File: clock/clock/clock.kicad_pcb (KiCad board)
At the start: 2 copper layers, 55 x 110 mm, 44 parts, among them J1 AVR-ISP-6, J10 Conn_01x05_Male, J11 CV_IN, J12 CLOCK_OUT, J13 SUBDIV_OUT, J2 EURORACK_CONN_10, J3 Conn_01x05_Female, J4 Conn_01x05_Male, J5 Conn_01x05_Female, J6 Conn_01x05_Male, J7 Conn_01x05_Female, J8 Conn_01x05_Male, J9 Conn_01x05_Female, SW1 SW_Push, SW2 SW_Push, SW3 SW_Coded_SH-7050, U1 ATmega328P-PU, U2 L7805, U3 SM460281N, U4 SM460281N, U5 SM460281N, Y1 16MHz

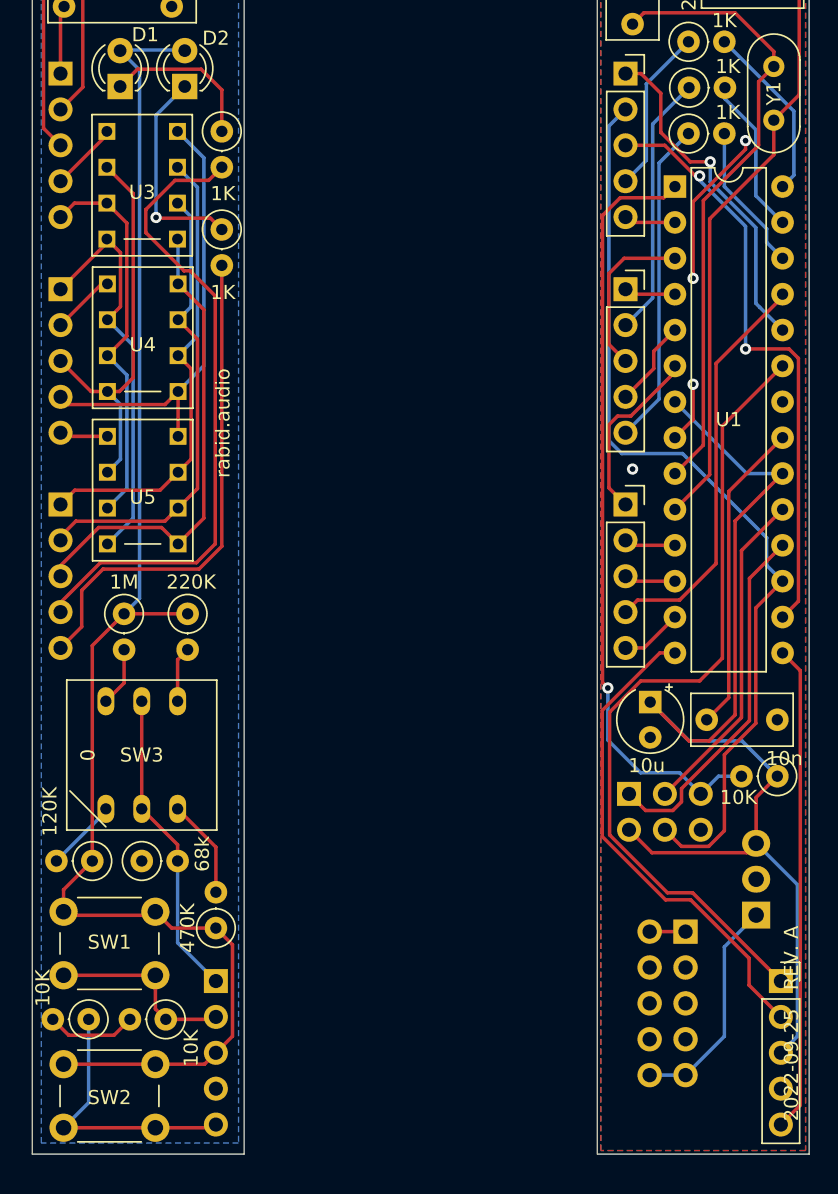
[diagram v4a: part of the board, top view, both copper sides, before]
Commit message: simplify some complex routing
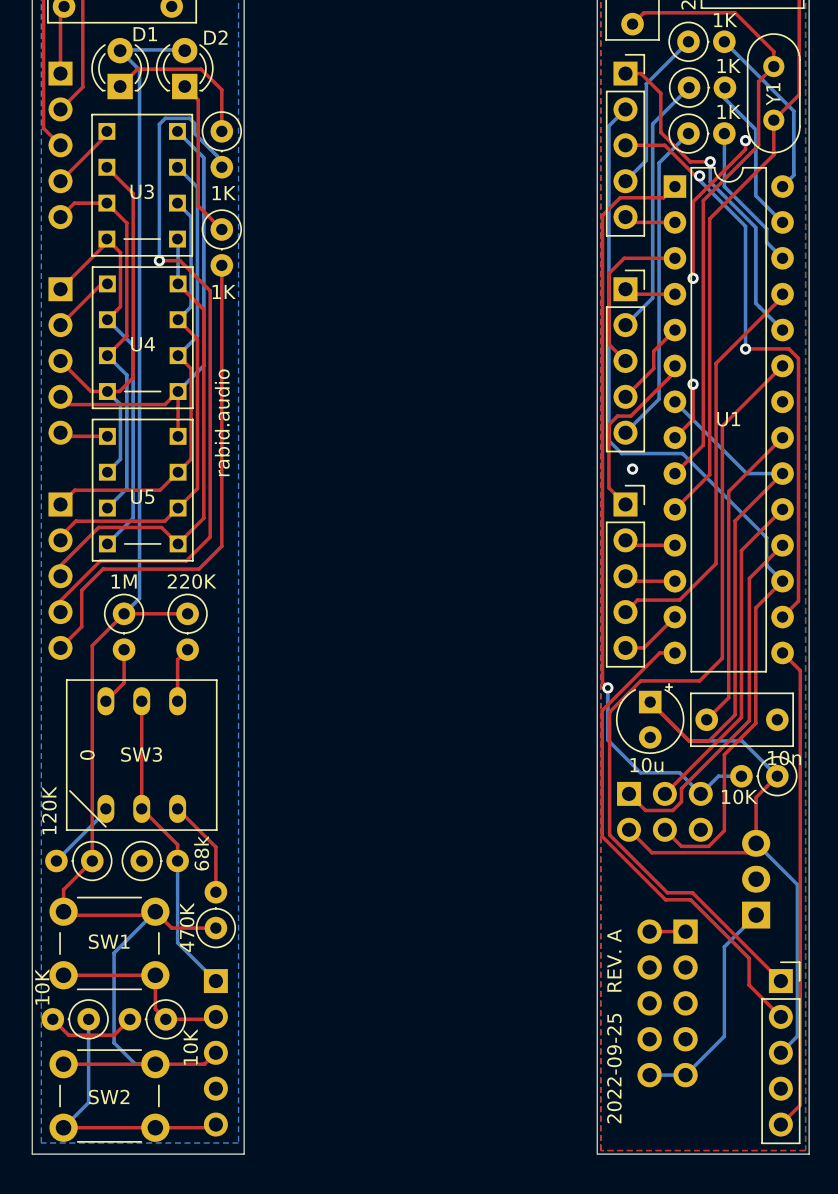
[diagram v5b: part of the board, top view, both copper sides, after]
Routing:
- net /LED_A: track 46.3 -> 52.6 mm, vias 0 -> 1
- net /AVCC: track 105.0 -> 109.3 mm
- net Net-(D2-Pad1): track 15.8 -> 11.9 mm, vias 1 -> 0
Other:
- board text removed: "TODO: confirm pot orientation"
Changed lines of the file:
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@@
   (general
     (thickness 1.6)
-    (drawings 13)
-    (tracks 342)
+    (drawings 12)
+    (tracks 344)
     (zones 0)
     (modules 44)
@@
     (effects (font (size 1 1) (thickness 0.15)) (justify mirror))
   )
-  (gr_text "2022-09-25   REV. A" (at 53.75 100.75 90) (layer F.SilkS)
+  (gr_text "2022-09-25   REV. A" (at 41.25 101 90) (layer F.SilkS)
     (effects (font (size 1 1) (thickness 0.15)))
   )
   (gr_text rabid.audio (at 13.5 58.25 90) (layer F.SilkS)
-    (effects (font (size 1 1) (thickness 0.15)))
-  )
-  (gr_text "TODO: confirm pot orientation" (at 12 117.5) (layer Dwgs.User)
     (effects (font (size 1 1) (thickness 0.15)))
   )
@@
   (segment (start 54.299999 35.000001) (end 54.299999 27.799999) (width 0.25) (layer F.Cu) (net 5))
   (segment (start 52.5 36.8) (end 54.299999 35.000001) (width 0.25) (layer F.Cu) (net 5) (status 10))
+  (segment (start 13.42 37.592) (end 13.42 34.656998) (width 0.25) (layer F.Cu) (net 6) (status 10))
+  (segment (start 13.42 34.656998) (end 11.955001 33.191999) (width 0.25) (layer F.Cu) (net 6))
   (segment (start 7.445001 33.191999) (end 6.22 34.417) (width 0.25) (layer F.Cu) (net 6) (status 20))
   (segment (start 11.955001 33.191999) (end 7.445001 33.191999) (width 0.25) (layer F.Cu) (net 6))
-  (segment (start 13.42 34.656998) (end 11.955001 33.191999) (width 0.25) (layer F.Cu) (net 6))
-  (segment (start 13.42 37.592) (end 13.42 34.656998) (width 0.25) (layer F.Cu) (net 6) (status 10))
   (segment (start 10.82 35.03) (end 10.82 34.37) (width 0.25) (layer F.Cu) (net 7) (status 30))
-  (segment (start 8.815001 43.740001) (end 8.763 43.688) (width 0.25) (layer F.Cu) (net 7))
-  (via (at 8.763 43.688) (size 0.8) (drill 0.4) (layers F.Cu B.Cu) (net 7))
-  (segment (start 12.620001 43.740001) (end 8.815001 43.740001) (width 0.25) (layer F.Cu) (net 7))
-  (segment (start 13.42 44.54) (end 12.620001 43.740001) (width 0.25) (layer F.Cu) (net 7) (status 10))
-  (segment (start 8.763 43.688) (end 8.763 36.449) (width 0.25) (layer B.Cu) (net 7))
-  (segment (start 8.763 36.449) (end 10.795 34.417) (width 0.25) (layer B.Cu) (net 7) (status 20))
+  (segment (start 13.42 44.54) (end 11.75 42.87) (width 0.25) (layer F.Cu) (net 7))
+  (segment (start 11.75 35.372) (end 10.795 34.417) (width 0.25) (layer F.Cu) (net 7))
+  (segment (start 11.75 42.87) (end 11.75 35.372) (width 0.25) (layer F.Cu) (net 7))
   (segment (start 44.704999 42.295001) (end 45.5 41.5) (width 0.25) (layer F.Cu) (net 8) (status 30))
   (segment (start 41.625997 42.295001) (end 44.704999 42.295001) (width 0.25) (layer F.Cu) (net 8) (status 20))
@@
   (segment (start 0.798999 6.470001) (end 0.798999 37.378999) (width 0.25) (layer F.Cu) (net 14))
   (segment (start 2.189 5.08) (end 0.798999 6.470001) (width 0.25) (layer F.Cu) (net 14) (status 10))
-  (segment (start 11.180001 47.464999) (end 12.954 49.238998) (width 0.25) (layer F.Cu) (net 15))
-  (segment (start 10.109997 41.060001) (end 8.037999 43.131999) (width 0.25) (layer F.Cu) (net 15))
-  (segment (start 13.42 40.132) (end 12.491999 41.060001) (width 0.25) (layer F.Cu) (net 15) (status 10))
-  (segment (start 12.491999 41.060001) (end 10.109997 41.060001) (width 0.25) (layer F.Cu) (net 15))
-  (segment (start 12.954 49.238998) (end 12.954 66.80059) (width 0.25) (layer F.Cu) (net 15))
-  (segment (start 12.954 66.80059) (end 11.6246 68.12999) (width 0.25) (layer F.Cu) (net 15))
-  (segment (start 8.037999 44.758001) (end 8.037999 43.131999) (width 0.25) (layer F.Cu) (net 15))
-  (segment (start 10.744997 47.464999) (end 8.037999 44.758001) (width 0.25) (layer F.Cu) (net 15))
-  (segment (start 11.180001 47.464999) (end 10.744997 47.464999) (width 0.25) (layer F.Cu) (net 15))
   (segment (start 2.105 71.885) (end 2.105 71.489998) (width 0.25) (layer F.Cu) (net 15) (status 30))
   (segment (start 2 70.958588) (end 2 71.628) (width 0.25) (layer F.Cu) (net 15) (status 30))
-  (segment (start 4.828597 68.129991) (end 2 70.958588) (width 0.25) (layer F.Cu) (net 15) (status 20))
-  (segment (start 11.6246 68.12999) (end 4.828597 68.129991) (width 0.25) (layer F.Cu) (net 15))
+  (segment (start 2 70.827002) (end 4.827002 68) (width 0.25) (layer F.Cu) (net 15))
+  (segment (start 2 71.628) (end 2 70.827002) (width 0.25) (layer F.Cu) (net 15))
+  (segment (start 10.910002 68) (end 12.595029 66.314973) (width 0.25) (layer F.Cu) (net 15))
+  (segment (start 4.827002 68) (end 10.910002 68) (width 0.25) (layer F.Cu) (net 15))
+  (segment (start 12.595029 66.314973) (end 12.595029 48.880027) (width 0.25) (layer F.Cu) (net 15))
+  (segment (start 13.42 40.132) (end 13.42 39.67) (width 0.25) (layer B.Cu) (net 15))
+  (segment (start 13.42 39.67) (end 11.5 37.75) (width 0.25) (layer B.Cu) (net 15))
+  (via (at 9 46.75) (size 0.8) (drill 0.4) (layers F.Cu B.Cu) (net 15))
+  (segment (start 11.140001 36.669999) (end 9.419999 36.669999) (width 0.25) (layer B.Cu) (net 15))
+  (segment (start 9 37.089998) (end 9 46.75) (width 0.25) (layer B.Cu) (net 15))
+  (segment (start 11.5 37.75) (end 11.5 37.029998) (width 0.25) (layer B.Cu) (net 15))
+  (segment (start 9.419999 36.669999) (end 9 37.089998) (width 0.25) (layer B.Cu) (net 15))
+  (segment (start 11.5 37.029998) (end 11.140001 36.669999) (width 0.25) (layer B.Cu) (net 15))
+  (segment (start 10.465002 46.75) (end 12.595029 48.880027) (width 0.25) (layer F.Cu) (net 15))
+  (segment (start 9 46.75) (end 10.465002 46.75) (width 0.25) (layer F.Cu) (net 15))
   (segment (start 13.42 66.971) (end 13.42 47.08) (width 0.25) (layer F.Cu) (net 16) (status 20))
   (segment (start 11.811 68.58) (end 13.42 66.971) (width 0.25) (layer F.Cu) (net 16))
@@
   (segment (start 12.194 103.636) (end 13 102.83) (width 0.25) (layer F.Cu) (net 31))
   (segment (start 8.715 103.636) (end 12.194 103.636) (width 0.25) (layer F.Cu) (net 31))
-  (segment (start 14.175001 95.175001) (end 13 94) (width 0.25) (layer F.Cu) (net 31))
-  (segment (start 14.175001 101.654999) (end 14.175001 95.175001) (width 0.25) (layer F.Cu) (net 31))
-  (segment (start 13 102.83) (end 14.175001 101.654999) (width 0.25) (layer F.Cu) (net 31))
   (segment (start 9.874 94) (end 8.715 92.841) (width 0.25) (layer F.Cu) (net 31))
   (segment (start 13 94) (end 9.874 94) (width 0.25) (layer F.Cu) (net 31))
@@
   (segment (start 4.25 74) (end 6.5 71.75) (width 0.25) (layer F.Cu) (net 31))
   (segment (start 4.25 89.25) (end 4.25 74) (width 0.25) (layer F.Cu) (net 31))
+  (segment (start 5.788999 102.124212) (end 5.788999 95.767001) (width 0.25) (layer B.Cu) (net 31))
+  (segment (start 5.788999 95.767001) (end 8.715 92.841) (width 0.25) (layer B.Cu) (net 31))
+  (segment (start 7.300787 103.636) (end 5.788999 102.124212) (width 0.25) (layer B.Cu) (net 31))
+  (segment (start 8.715 103.636) (end 7.300787 103.636) (width 0.25) (layer B.Cu) (net 31))
   (segment (start 41.737999 60.405001) (end 40.824999 59.492001) (width 0.25) (layer B.Cu) (net 32))
   (segment (start 46.040001 60.405001) (end 41.737999 60.405001) (width 0.25) (layer B.Cu) (net 32))

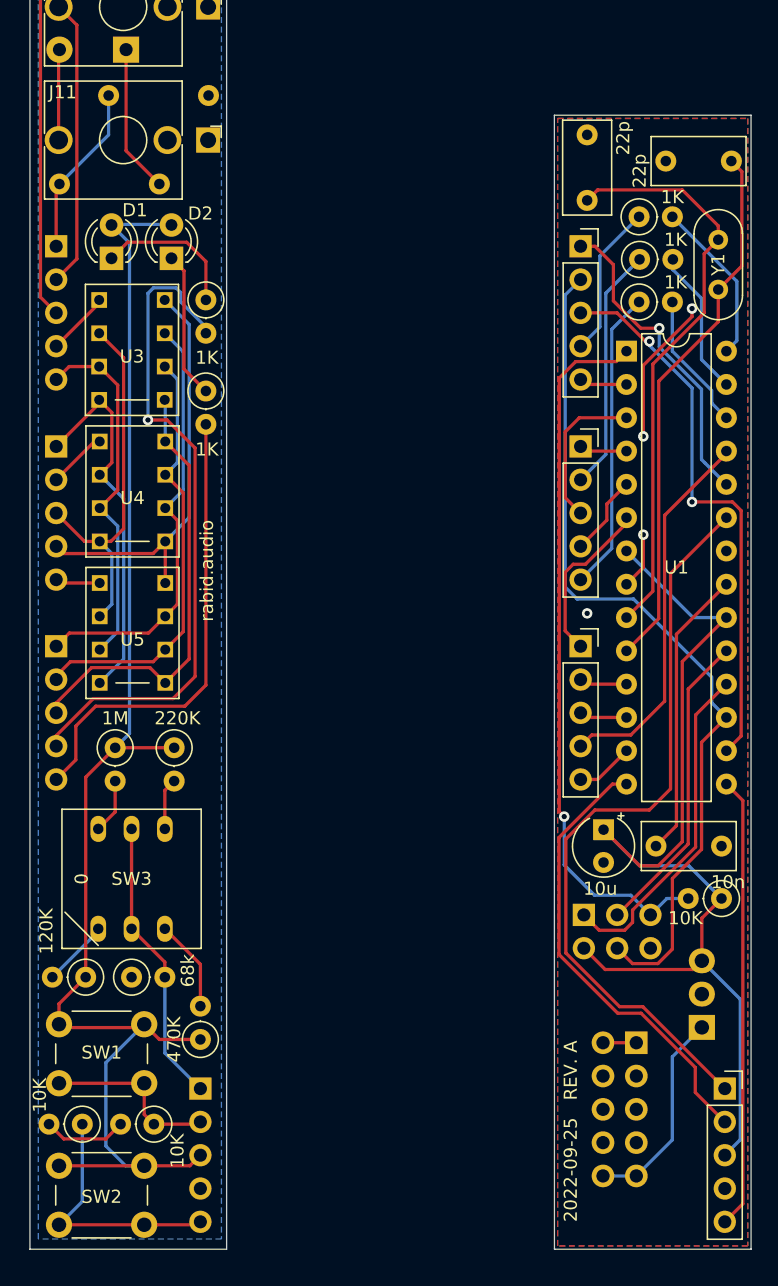
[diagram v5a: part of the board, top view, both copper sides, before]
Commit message: redesign pcb around rotary encoder
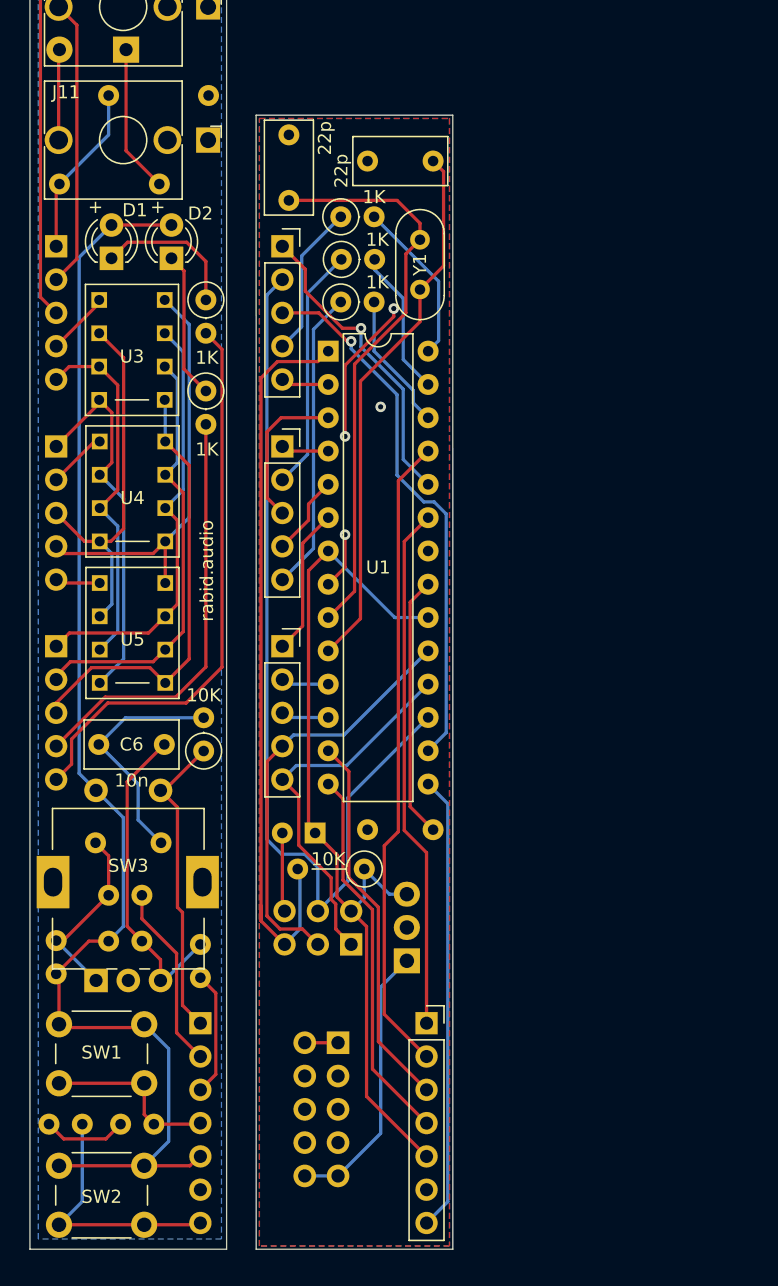
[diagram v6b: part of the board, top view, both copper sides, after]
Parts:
- added C5: 10n, Capacitor_THT:C_Rect_L7.0mm_W3.5mm_P5.00mm, B.Cu at (5.00, 79.0)
- added C6: 10n, Capacitor_THT:C_Rect_L7.0mm_W3.5mm_P5.00mm, F.Cu at (10.2, 71.5)
- C1, C2, R4, R5: moved to B.Cu
- J1: value AVR-ISP-6 -> AVR-ISP
- J10: value Conn_01x05_Male -> Conn_01x07_Male; footprint Connector_PinHeader_2.54mm:PinHeader_1x05_P2.54mm_Vertical -> Connector_PinHeader_2.54mm:PinHeader_1x07_P2.54mm_Vertical
- J9: value Conn_01x05_Female -> Conn_01x07_Female; footprint Connector_PinSocket_2.54mm:PinSocket_1x05_P2.54mm_Vertical -> Connector_PinSocket_2.54mm:PinSocket_1x07_P2.54mm_Vertical
- R1: footprint Resistor_THT:R_Axial_DIN0207_L6.3mm_D2.5mm_P2.54mm_Vertical -> Resistor_THT:R_Axial_DIN0207_L6.3mm_D2.5mm_P5.08mm_Vertical
- R10: value 220K -> 10K; moved to B.Cu
- R11: value 470K -> 10K; moved to B.Cu
- R12: value 1M -> 10K; moved to B.Cu
- R13: value 68k -> 10K
- R9: value 120K -> 10K; moved to B.Cu
- SW3: value SW_Coded_SH-7050 -> Rotary_Encoder_Switch; footprint synth:SD-1110 -> synth:RotaryEncoder_Bourns_PEC11H_Vertical_Switch
- moved R1 27.3 mm to (25.5, 81.0)
- moved C2 27.0 mm to (25.8, 78.0), turned to 0 degrees
- moved J9 23.3 mm to (30.2, 92.8)
- moved U2 23.1 mm to (28.8, 88.0)
- moved C3 22.8 mm to (19.8, 25.0)
- moved C4 22.8 mm to (25.8, 27.0)
- moved J2 22.8 mm to (23.5, 94.2)
- moved J3 22.8 mm to (19.2, 33.5)
- moved J5 22.8 mm to (19.2, 48.8)
- moved J7 22.8 mm to (19.2, 64.0)
- moved R6 22.8 mm to (23.7, 37.8)
- moved R7 22.8 mm to (23.8, 34.5)
- moved R8 22.8 mm to (23.7, 31.2)
- moved U1 22.8 mm to (22.8, 41.5)
- moved Y1 22.8 mm to (29.8, 33.0)
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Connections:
- net /B_KNOB renamed /B_SW3
- J1 pad 1: /MISO -> /B_LEDL
- J1 pad 3: /SCK -> /B_LEDR
- J10 pad 1: /KNOB -> /SW3
- J10 pad 2: /SW1 -> /KNOBL
- J10 pad 3: /AVCC -> /KNOBR
- J10 pad 4: /AGND -> /SW1
- J10 pad 5: /SW2 -> /AVCC
- J7 pad 4: /B_LED_A -> /B_LEDR
- J7 pad 5: /B_LED_B -> /B_LEDL
- J8 pad 4: /LED_A -> /LEDR
- J8 pad 5: /LED_B -> /LEDL
- J9 pad 2: /B_SW1 -> /B_KNOBL
- J9 pad 3: +5V -> /B_KNOBR
- J9 pad 4: GND -> /B_SW1
- J9 pad 5: /B_SW2 -> +5V
- R10 pad 2: Net-(R10-Pad2) -> Net-(C5-Pad1)
- R11 pad 2: Net-(R11-Pad2) -> Net-(C6-Pad1)
- R12 pad 1: /AVCC -> Net-(C6-Pad1)
- R12 pad 2: Net-(R12-Pad2) -> /KNOBR
- R13 pad 1: /AGND -> /SW3
- R13 pad 2: /KNOB -> /AGND
- R2 pad 2: /LED_A -> /LEDL
- R3 pad 2: /LED_B -> /LEDR
- R9 pad 1: /AVCC -> Net-(C5-Pad1)
- R9 pad 2: Net-(R9-Pad2) -> /KNOBL
- SW3 pad 1: Net-(R9-Pad2) -> Net-(C5-Pad1)
- SW3 pad 2: Net-(R10-Pad2) -> /AGND
- SW3 pad 4: Net-(R11-Pad2) -> /SW3
- U1 pad 13: /B_LED_B -> /B_KNOBR
- U1 pad 18: /MISO -> /B_LEDL
- U1 pad 19: /SCK -> /B_LEDR
- U1 pad 25: /B_LED_A -> /B_KNOBL
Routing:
- net /LED_A: track 52.6 -> 0.00 mm, vias 1 -> 0
- net /B_KNOBL: track 0.00 -> 48.9 mm
- net /LEDL: track 0.00 -> 43.3 mm
- net /LED_B: track 35.8 -> 0.00 mm
- net /LEDR: track 0.00 -> 33.1 mm
- net /B_LEDR: track 0.00 -> 32.4 mm
- net /B_KNOBR: track 0.00 -> 29.0 mm
- net /B_LEDL: track 0.00 -> 28.9 mm
- net /B_LED_A: track 28.9 -> 0.00 mm
- net /MISO: track 25.6 -> 0.00 mm
- net Net-(C6-Pad1): track 0.00 -> 25.4 mm
- net /SW3: track 0.00 -> 23.8 mm
- net /SCK: track 23.6 -> 0.00 mm
- net /KNOB: track 22.0 -> 0.00 mm
- net /AGND: track 6.39 -> 24.7 mm
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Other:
- board size 55 x 110 mm -> 32.3 x 110 mm
- board text added: "+"
- board text added: "2022-11-24 REV. A"
- board text removed: "2022-09-25 REV. A"

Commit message: make a bit more space
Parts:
- J1: value AVR-ISP -> ISP
- R1: moved to B.Cu
- moved R1 6.18 mm to (24.0, 87.0)
- moved J1 3.25 mm to (24.5, 83.5)
- moved U1 2.51 mm to (23.0, 39.0)
- moved Y1 2.51 mm to (30.0, 30.5)
- moved C1 2.15 mm to (23.0, 76.5)
- moved R6 2.02 mm to (24.0, 35.8)
- moved R8 2.02 mm to (24.0, 29.2)
- moved R7 2.02 mm to (24.0, 32.5)
- moved C4 1.52 mm to (26.0, 25.5)
- moved C2 1.50 mm to (25.8, 76.5)
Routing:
- net GND: track 21.6 -> 12.6 mm, vias 4 -> 2
- net /B_SUBDIV_OUT: track 70.7 -> 63.7 mm
- net /B_SW3: track 40.0 -> 42.6 mm
- net /B_LED3: track 6.18 -> 8.78 mm
- net /B_KNOBL: track 48.9 -> 51.5 mm
- net /B_KNOBR: track 29.0 -> 31.4 mm
- net /B_SW1: track 29.0 -> 31.4 mm
- net /B_LED4: track 11.7 -> 13.9 mm
- net /B_LED_C3: track 23.0 -> 25.1 mm
- net /B_LED_C1: track 11.7 -> 13.8 mm
- net /B_LED_C2: track 18.7 -> 20.8 mm
- net /B_CV_IN: track 24.3 -> 22.4 mm
- net Net-(R8-Pad2): track 13.2 -> 11.4 mm
- net /B_SW2: track 35.5 -> 37.2 mm
- net /B_LEDR: track 32.4 -> 34.0 mm
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
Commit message: fix PCB
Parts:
- removed R12, R9: 10K, Resistor_THT:R_Axial_DIN0207_L6.3mm_D2.5mm_P2.54mm_Vertical
- C3, C4, C6, R6, R7, R8, Y1: moved to B.Cu
- J1: value ISP -> AVR-ISP-6
- SW3: footprint synth:RotaryEncoder_Bourns_PEC11H_Vertical_Switch -> synth:RotaryEncoder_Bourns_PEC11R_Vertical_Switch
- moved C3 0.35 mm to (19.5, 25.2)
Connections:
- C5 pad 1: Net-(C5-Pad1) -> /KNOBL
- C6 pad 1: Net-(C6-Pad1) -> /KNOBR
- D1 pad 1: Net-(D1-Pad1) -> /AGND
- D1 pad 2: /AVCC -> Net-(D1-Pad2)
- D2 pad 1: Net-(D2-Pad1) -> /AGND
- D2 pad 2: /AVCC -> Net-(D2-Pad2)
- J10 pad 1: /SW3 -> /KNOBR
- J10 pad 3: /KNOBR -> /SW3
- J9 pad 1: /B_SW3 -> /B_KNOBR
- J9 pad 3: /B_KNOBR -> /B_SW3
- R10 pad 2: Net-(C5-Pad1) -> /KNOBL
- R11 pad 2: Net-(C6-Pad1) -> /KNOBR
- R2 pad 1: Net-(D1-Pad1) -> Net-(D1-Pad2)
- R3 pad 1: Net-(D2-Pad1) -> Net-(D2-Pad2)
- SW3 pad 1: Net-(C5-Pad1) -> /KNOBL
- SW3 pad 3: Net-(C6-Pad1) -> /KNOBR
- U1 pad 13: /B_KNOBR -> /B_SW3
- U1 pad 23: /B_SW3 -> /B_KNOBR
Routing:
- net Net-(C6-Pad1): track 25.4 -> 0.00 mm
- net /KNOBR: track 9.52 -> 25.9 mm
- net Net-(C5-Pad1): track 14.7 -> 0.00 mm
- net Net-(D2-Pad2): track 0.00 -> 13.8 mm
- net Net-(D1-Pad2): track 0.00 -> 13.5 mm
- net Net-(D2-Pad1): track 11.9 -> 0.00 mm
- net /B_SW3: track 42.6 -> 31.4 mm
- net /B_KNOBR: track 31.4 -> 42.6 mm
- net Net-(D1-Pad1): track 11.2 -> 0.00 mm
- net /KNOBL: track 14.1 -> 24.6 mm
- net /AVCC: track 101.0 -> 92.7 mm
- net /SW3: track 23.8 -> 29.9 mm
- net /AGND: track 24.7 -> 22.4 mm
